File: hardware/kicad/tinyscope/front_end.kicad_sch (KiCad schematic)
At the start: 29 parts, among them J6 Front End A, J7 Front End B, U13 AD8066ARZ-RL, U14 AD8066ARZ-RL, U15 AD8066ARZ-RL

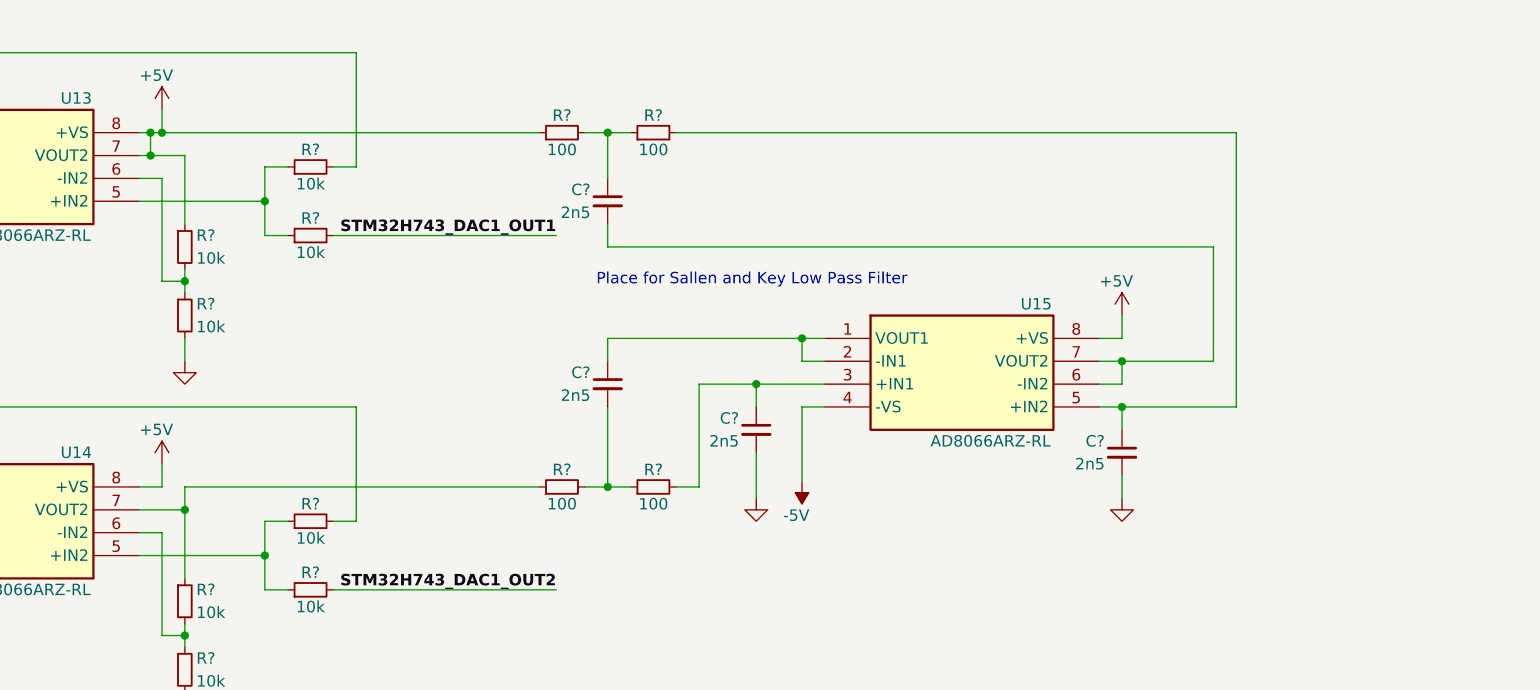
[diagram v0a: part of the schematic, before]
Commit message: feat: hardware: note: Changes the caps values of two Sallen and Key Low Pass Filters (anti-aliasing) to match Butterworth filter
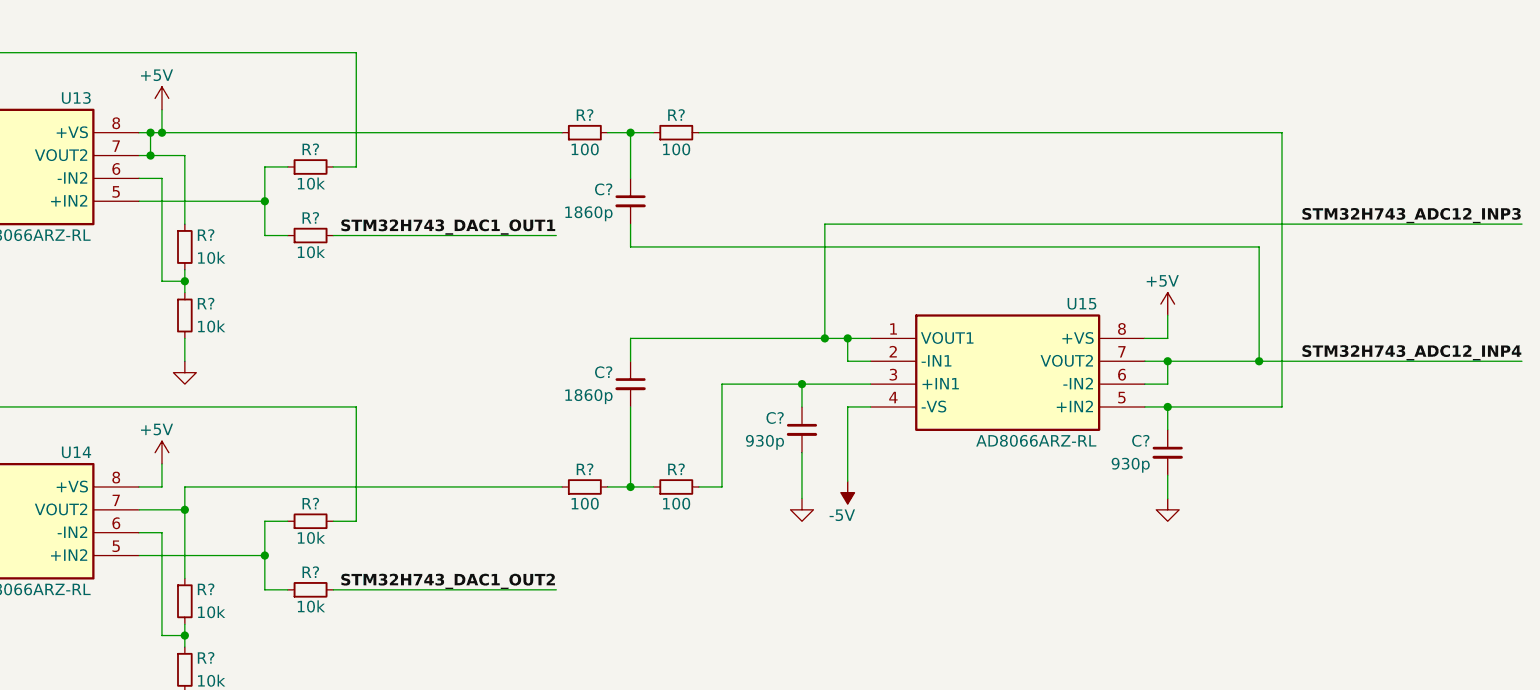
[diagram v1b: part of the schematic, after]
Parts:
- C? (x2): value 2n5 -> 930p
- C? (x2): value 2n5 -> 1860p
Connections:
- net STM32H743_ADC12_INP3: now reaches C?.1, U15.1 (VOUT1), U15.2 (-IN1)
- net STM32H743_ADC12_INP4: now reaches C?.2, U15.6 (-IN2), U15.7 (VOUT2)
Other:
- note removed: "Place for Sallen and Key Low Pass Filter"
- moved on the sheet: C?, R?, U15

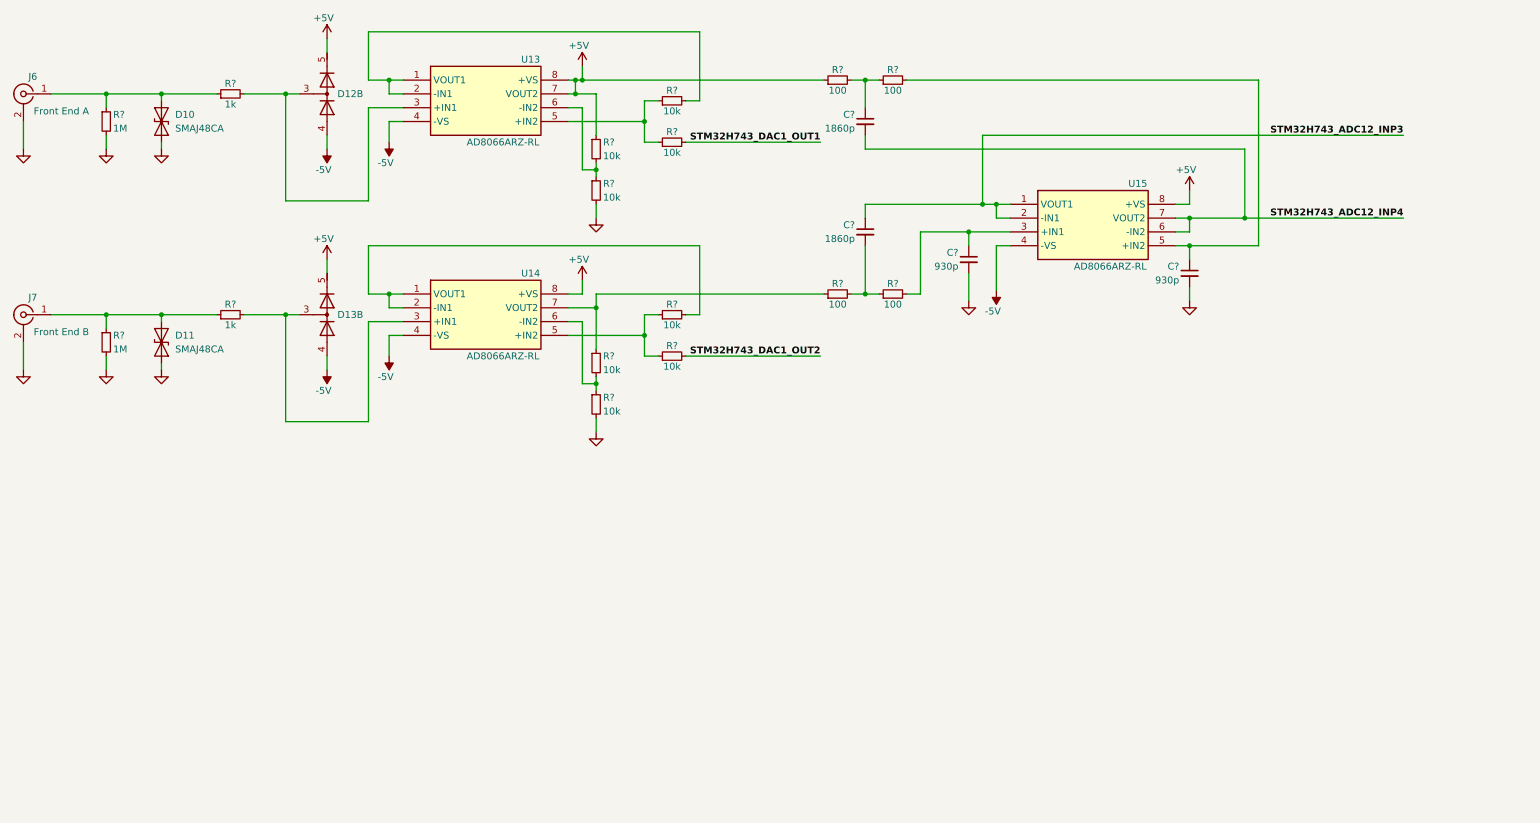
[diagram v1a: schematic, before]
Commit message: feat: hardware: Adds decoupling capacitors for op amps and front end description
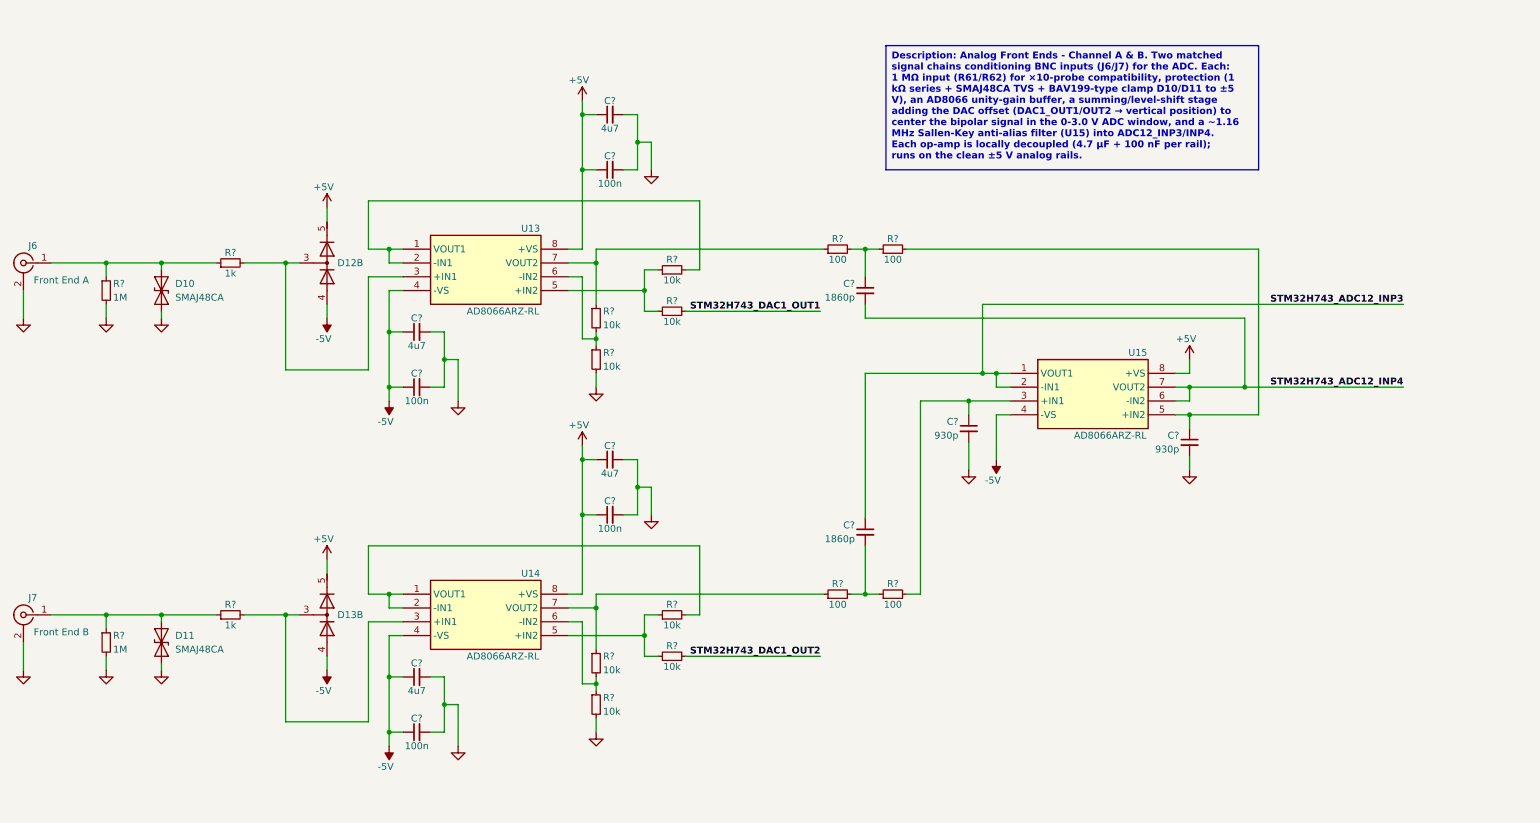
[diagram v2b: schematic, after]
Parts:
- added C? (x4): 4u7, symbol Device:C_Small
- added C? (x4): 100n, symbol Device:C_Small
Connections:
- net +5V: now also C?.1, C?.1, C?.1, C?.1; no longer R?.1, R?.1, U13.7 (VOUT2)
- net -5V: now also C?.1, C?.1, C?.1, C?.1
- net GND: now also C?.2, C?.2, C?.2, C?.2, C?.2, C?.2, C?.2, C?.2
- new net: R?.1, R?.1, U13.7 (VOUT2)
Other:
- moved on the sheet: C?, D10, D11, D12B, D13B, J6, J7, R?, U13, U14, U15

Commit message: feat: hardware: doc: Modifies placement for the schematic description
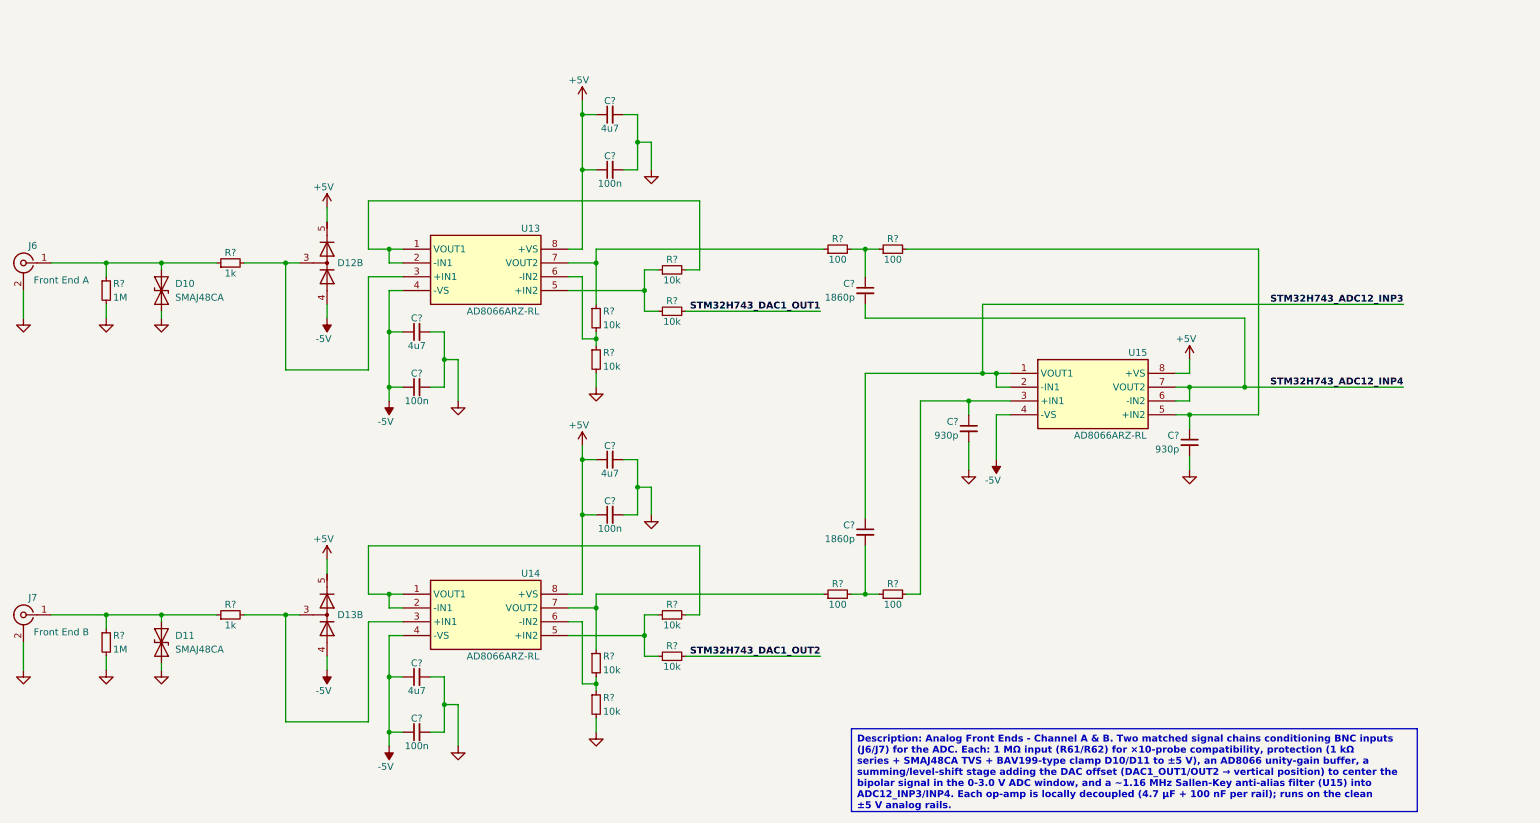
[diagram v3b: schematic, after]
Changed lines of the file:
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@@
   )
   (text_box "Description: Analog Front Ends - Channel A & B. Two matched signal chains conditioning BNC inputs (J6/J7) for the ADC. Each: 1 MΩ input (R61/R62) for ×10-probe compatibility, protection (1 kΩ series + SMAJ48CA TVS + BAV199-type clamp D10/D11 to ±5 V), an AD8066 unity-gain buffer, a summing/level-shift stage adding the DAC offset (DAC1_OUT1/OUT2 → vertical position) to center the bipolar signal in the 0-3.0 V ADC window, and a ~1.16 MHz Sallen-Key anti-alias filter (U15) into ADC12_INP3/INP4. Each op-amp is locally decoupled (4.7 µF + 100 nF per rail); runs on the clean ±5 V analog rails."
-    (at 184.15 21.59 0) (size 68.58 22.86)
+    (at 177.8 147.32 0) (size 104.14 15.24)
     (stroke (width 0) (type default))
     (fill (type color) (color 255 255 194 1))
